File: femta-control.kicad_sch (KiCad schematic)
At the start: 19 parts, among them J1 CUBESAT INTERFACE

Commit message: work
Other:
- added sheet Valves (valve-master.kicad_sch)
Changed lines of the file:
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@@
+	)
+	(sheet
+		(at 292.1 91.44)
+		(size 40.64 29.21)
+		(fields_autoplaced yes)
+		(stroke
+			(width 0.1524)
+			(type solid)
+		)
+		(fill
+			(color 0 0 0 0.0000)
+		)
+		(property "Sheetname" "Valves"
+			(at 292.1 90.7284 0)
+			(effects
+				(font
+					(size 1.27 1.27)
+				)
+				(justify left bottom)
+			)
+		)
+		(property "Sheetfile" "valve-master.kicad_sch"
+			(at 292.1 121.2346 0)
+			(effects
+				(font
+					(size 1.27 1.27)
+				)
+				(justify left top)
+			)
+		)
+		(instances
+			(project "femta-control"
+				(path "/838bf11c-36b7-41d7-9462-fe98a188d617"
+					(page "31")
+				)
+			)
+		)
 	)
 	(sheet

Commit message: lots and lots and lots of work
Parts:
- added C94, C95: 10uF, symbol Device:C
- added U92: NCV1117-12_SOT223, Package_TO_SOT_SMD:SOT-223-3_TabPin2, symbol Regulator_Linear:NCP1117-12_SOT223
- R11: value 10K -> 24K
- R13: value 30K -> 24K
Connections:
- net +BATT: now also C94.1, U92.3 (VI)
- net GND: now also C94.2, C95.1, U92.1 (GND)
- new net +12V: C95.2, U92.2 (VO)
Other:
- sheet DPT Sensors renamed DPT and Flow
- sheet DPT and Flow: file dpt.kicad_sch -> dpt-flow.kicad_sch
- note added: "0.6A Limit on 3.3V Rail"
- note added: "0.6A Limit on 5V Rail"
- note added: "2.04A Limit on Batt Rail"
- note added: "2.04A Limit on Heater Rail"

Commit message: work
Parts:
- added JP2: HEATER_POWER, symbol Jumper:SolderJumper_2_Open
- added TP1: 5VTP, symbol Connector:TestPoint
- added TP2: 3V3TP, symbol Connector:TestPoint
- added TP3: 5VPTP, symbol Connector:TestPoint
- added TP4: BATTTP, symbol Connector:TestPoint
- added TP5: GNDTP, symbol Connector:TestPoint
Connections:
- net +3.3V: now also TP2.1
- net +5V: now also TP1.1
- net +5VP: now also TP3.1
- net +BATT: now also TP4.1
- net 5V_HEATER_UNPROT: now also JP2.2 (B)
- net 5V_UNPROT: now also JP2.1 (A)
- net GND: now also TP5.1
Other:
- note added: "Power indicators & Test Points"
- note removed: "Power indicators"

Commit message: 540 COMPONENTS I AM LOSING MY MINDDDDDD
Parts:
- added C3, C5, C6: 0.1uF, symbol Device:C
- added C4: 1uF, symbol Device:C
- added U2: MAX6103, Package_TO_SOT_SMD:SOT-23, symbol Reference_Voltage:MAX6103
- added U3: MCP3204, Package_SO:TSSOP-14_4.4x5mm_P0.65mm, symbol Analog_ADC:MCP3204
- TP1: footprint (none) -> TestPoint:TestPoint_Pad_D2.0mm
- TP2: renamed from TP5; footprint (none) -> TestPoint:TestPoint_Pad_D2.0mm
- TP3: renamed from TP2; footprint (none) -> TestPoint:TestPoint_Pad_D2.0mm
- TP4: renamed from TP3; footprint (none) -> TestPoint:TestPoint_Pad_D2.0mm
- TP5: renamed from TP4; footprint (none) -> TestPoint:TestPoint_Pad_D2.0mm
- renumbered C94 to C1, C95 to C2, JP2 to JP1, R6 to R1, R9 to R10, R7 to R2, R8 to R3, R10 to R4, R1 to R5, R2 to R6, R3 to R7, R4 to R8, R5 to R9, U92 to U1
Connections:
- net +3.3V: now also C6.1, U3.14 (Vdd)
- net +5V: now also C3.1, U2.1 (IN)
- net GND: now also C3.2, C4.2, C5.2, C6.2, U2.3 (GND), U3.12 (AGND), U3.3 (CH2), U3.4 (CH3), U3.7 (DGND)
- new net 3V_REF: C4.1, C5.1, U2.2 (OUT), U3.13 (Vref)
- new net I_TELEM_CS: U3.8 (~{CS}/SHDN)
- new net POUT_1: U3.1 (CH0)
- new net POUT_2: U3.2 (CH1)
- new net SPI_CLK: U3.11 (CLK)
- new net SPI_MISO: U3.10 (Dout)
- new net SPI_MOSI: U3.9 (Din)
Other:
- sheet Thermal Circuits ports: added 165_CS, 595_CS, EN_OUT_595, LOAD_165, LOAD_595, P_ADC_CS, SPI_CLK, SPI_MISO, SPI_MOSI, TSET_CS, T_ADC_CS; removed none
- sheet Thrust Control Side 1 ports: added POUT_CS, PSET_CS, SPI_CLK, SPI_MISO, SPI_MOSI; removed none
- sheet Thrust Control Side 2 ports: added POUT_CS, PSET_CS, SPI_CLK, SPI_MISO, SPI_MOSI; removed none
- sheet Thruster Control Main ports: added POUT_CS, PSET_CS, SPI_CLK, SPI_MISO, SPI_MOSI; removed none
- sheet Valves ports: added 595_CS, EN_OUT_595, LOAD_595, SPI_CLK, SPI_MOSI; removed none
- moved on the sheet: C1, C2, D1, D2, D3, D4, J1, JP1, R1, R10, R11, R12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

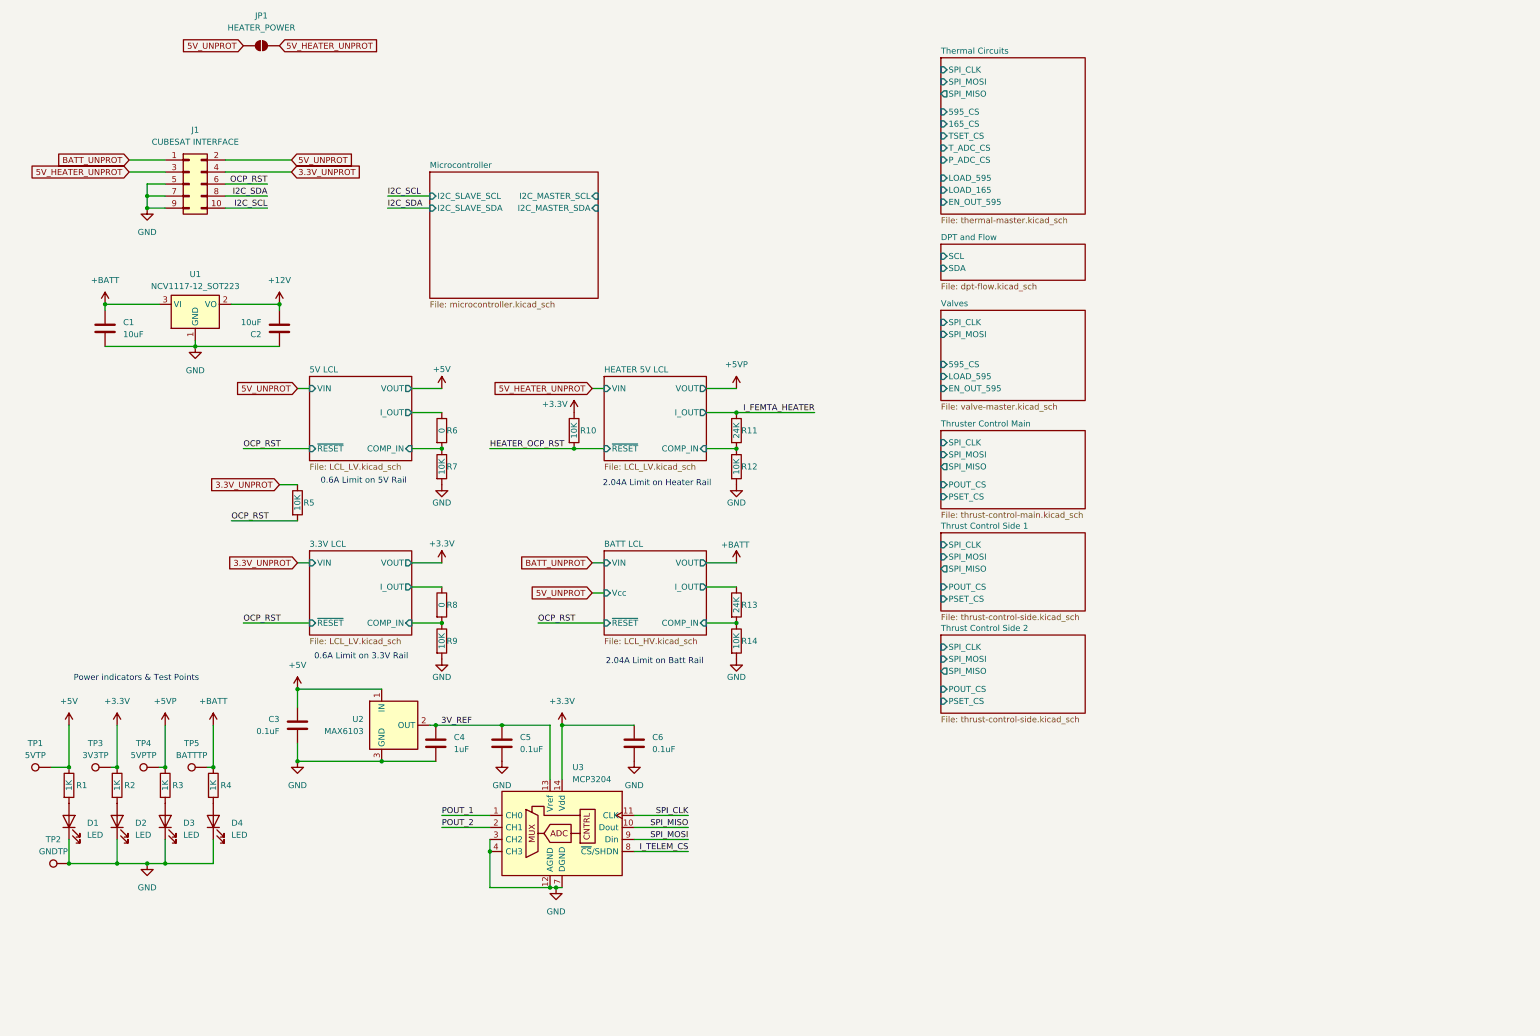
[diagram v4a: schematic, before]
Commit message: page sizes
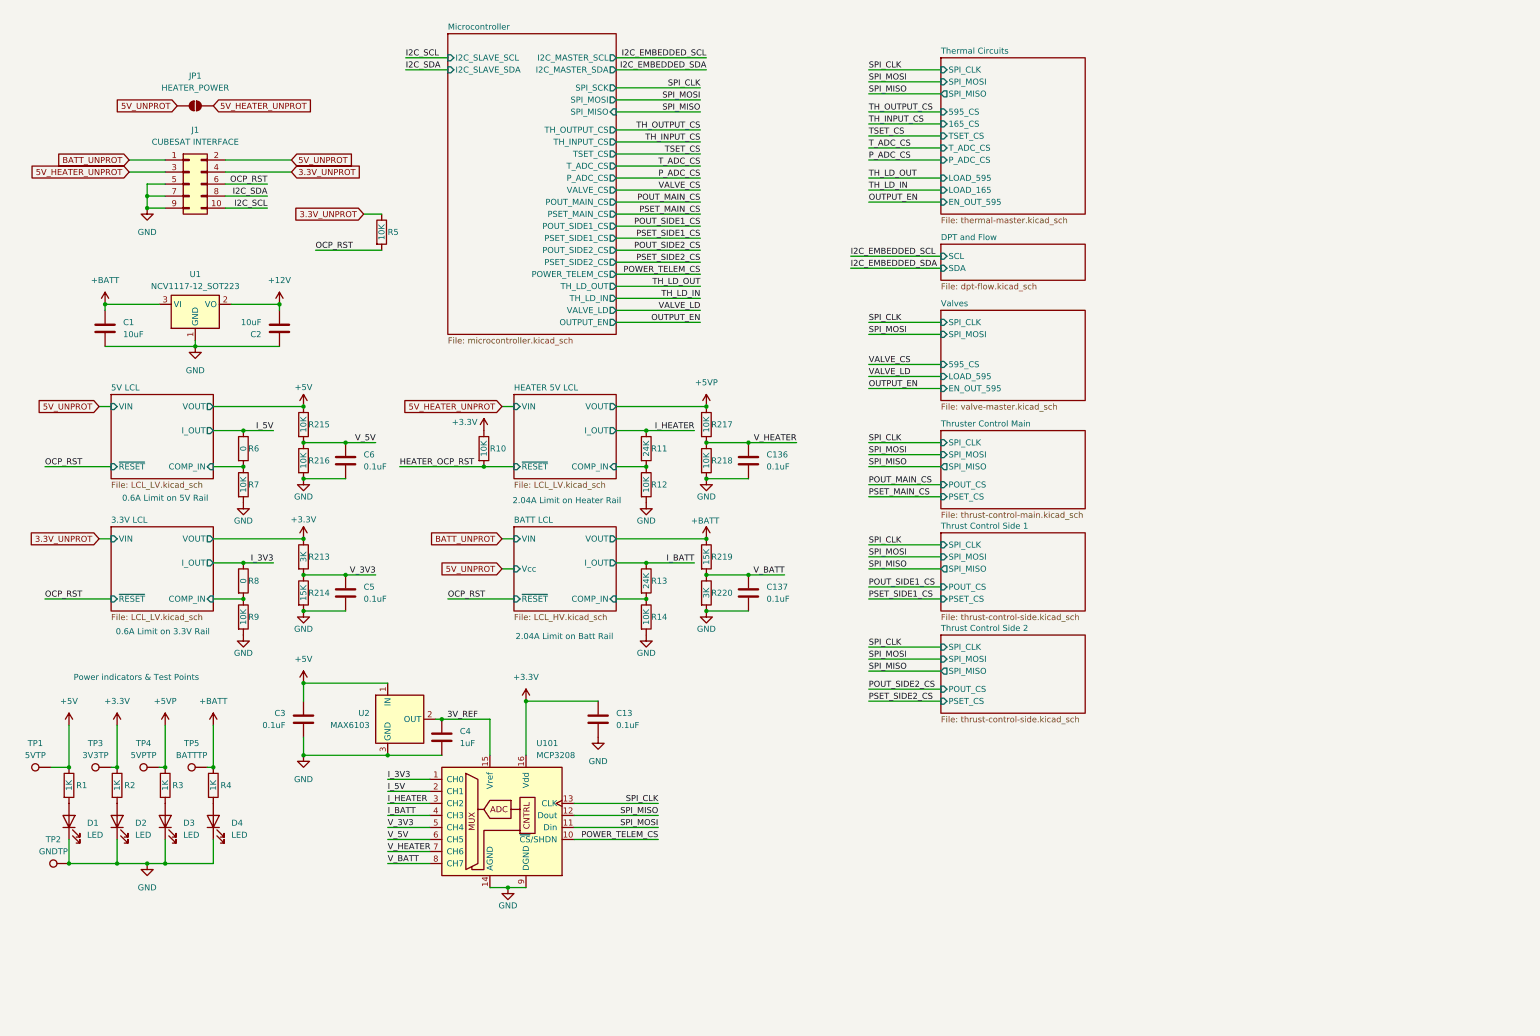
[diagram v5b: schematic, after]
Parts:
- removed U3: MCP3204, Package_SO:TSSOP-14_4.4x5mm_P0.65mm, symbol Analog_ADC:MCP3204
- added C13, C136, C137: 0.1uF, symbol Device:C
- added R213, R220: 3K, symbol Device:R
- added R214, R219: 15K, symbol Device:R
- added R215, R216, R217, R218: 10K, symbol Device:R
- added U101: MCP3208, Package_SO:SOIC-16_3.9x9.9mm_P1.27mm, symbol Analog_ADC:MCP3208
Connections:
- net +3.3V: now also C13.1, R213.1, U101.16 (Vdd); no longer C6.1
- net +5V: now also R215.1
- net +5VP: now also R217.1
- net +BATT: now also R219.1
- net 3V_REF: now also U101.15 (Vref); no longer C5.1
- net GND: now also C13.2, C136.2, C137.2, R214.2, R216.2, R218.2, R220.2, U101.14 (AGND), U101.9 (DGND)
- net SPI_CLK: now also U101.13 (CLK)
- net SPI_MISO: now also U101.12 (Dout)
- net SPI_MOSI: now also U101.11 (Din)
- net 3.3V LCL/I_OUT renamed I_3V3
- net I_3V3: now also U101.1 (CH0)
- net 5V LCL/I_OUT renamed I_5V
- net I_5V: now also U101.2 (CH1)
- net BATT LCL/I_OUT renamed I_BATT
- net I_BATT: now also U101.4 (CH3)
- net I_FEMTA_HEATER renamed I_HEATER
- net I_HEATER: now also U101.3 (CH2)
- new net POWER_TELEM_CS: U101.10 (~{CS}/SHDN)
- new net V_3V3: C5.1, R213.2, R214.1, U101.5 (CH4)
- new net V_5V: C6.1, R215.2, R216.1, U101.6 (CH5)
- new net V_BATT: C137.1, R219.2, R220.1, U101.8 (CH7)
- new net V_HEATER: C136.1, R217.2, R218.1, U101.7 (CH6)
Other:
- sheet Microcontroller ports: added OUTPUT_EN, POUT_MAIN_CS, POUT_SIDE1_CS, POUT_SIDE2_CS, POWER_TELEM_CS, PSET_MAIN_CS, PSET_SIDE1_CS, PSET_SIDE2_CS, P_ADC_CS, SPI_MISO, SPI_MOSI, SPI_SCK, TH_INPUT_CS, TH_LD_IN, TH_LD_OUT, TH_OUTPUT_CS, TSET_CS, T_ADC_CS, VALVE_CS, VALVE_LD; removed none
- moved on the sheet: C3, C4, JP1, R10, R11, R12, R13, R14, R5, R6, R7, R8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

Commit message: schematic finished milestone
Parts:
- renumbered C6 to C4, C4 to C6, C13 to C7, C136 to C8, C137 to C9, R216 to R10, R213 to R11, R214 to R12, R5 to R13, R10 to R14, R11 to R15, R12 to R16, R13 to R17, R14 to R18, R217 to R19, R218 to R20, R219 to R21, R220 to R22, R6 to R5, R7 to R6, R8 to R7, R9 to R8, R215 to R9, U101 to U3

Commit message: capacitor footprints
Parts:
- C1, C2: footprint (none) -> Capacitor_SMD:C_1210_3225Metric
- C3, C4, C5, C6, C7, C8, C9: footprint (none) -> Capacitor_SMD:C_0603_1608Metric
- D1, D2, D3, D4: footprint (none) -> Diode_SMD:D_0603_1608Metric
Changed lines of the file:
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@@
 			)
 		)
-		(property "Footprint" ""
+		(property "Footprint" "Capacitor_SMD:C_0603_1608Metric"
 			(at 141.9352 165.1 0)
 			(effects
@@
 			)
 		)
-		(property "Footprint" ""
+		(property "Footprint" "Capacitor_SMD:C_0603_1608Metric"
 			(at 88.5952 138.43 0)
 			(effects
@@
 			)
 		)
-		(property "Footprint" ""
+		(property "Footprint" "Capacitor_SMD:C_0603_1608Metric"
 			(at 173.6852 110.49 0)
 			(effects
@@
 			)
 		)
-		(property "Footprint" ""
+		(property "Footprint" "Capacitor_SMD:C_0603_1608Metric"
 			(at 173.6852 138.43 0)
 			(effects
@@
 			)
 		)
-		(property "Footprint" ""
+		(property "Footprint" "Diode_SMD:D_0603_1608Metric"
 			(at 49.53 182.88 0)
 			(effects
@@
 			)
 		)
-		(property "Footprint" ""
+		(property "Footprint" "Diode_SMD:D_0603_1608Metric"
 			(at 29.21 182.88 0)
 			(effects
@@
 			)
 		)
-		(property "Footprint" ""
+		(property "Footprint" "Diode_SMD:D_0603_1608Metric"
 			(at 39.37 182.88 0)
 			(effects
@@
 			)
 		)
-		(property "Footprint" ""
+		(property "Footprint" "Capacitor_SMD:C_0603_1608Metric"
 			(at 108.9152 168.91 0)
 			(effects
@@
 			)
 		)
-		(property "Footprint" ""
+		(property "Footprint" "Diode_SMD:D_0603_1608Metric"
 			(at 59.69 182.88 0)
 			(effects
@@
 			)
 		)
-		(property "Footprint" ""
+		(property "Footprint" "Capacitor_SMD:C_1210_3225Metric"
 			(at 37.7952 82.55 0)
 			(effects
@@
 			)
 		)
-		(property "Footprint" ""
+		(property "Footprint" "Capacitor_SMD:C_0603_1608Metric"
 			(at 79.7052 165.1 0)
 			(effects
@@
 			)
 		)
-		(property "Footprint" ""
+		(property "Footprint" "Capacitor_SMD:C_1210_3225Metric"
 			(at 72.6948 74.93 0)
 			(effects
@@
 			)
 		)
-		(property "Footprint" ""
+		(property "Footprint" "Capacitor_SMD:C_0603_1608Metric"
 			(at 88.5952 110.49 0)
 			(effects

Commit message: add more footprints
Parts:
- R1, R10, R11, R12, R13, R14, R15, R16, R17, R18, R19, R2, R20, R21, R22, R3, R4, R5, R6, R7, R8, R9: footprint (none) -> Resistor_SMD:R_0603_1608Metric
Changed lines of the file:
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@@
 			)
 		)
-		(property "Footprint" ""
+		(property "Footprint" "Resistor_SMD:R_0603_1608Metric"
 			(at 64.262 132.08 90)
 			(effects
@@
 			)
 		)
-		(property "Footprint" ""
+		(property "Footprint" "Resistor_SMD:R_0603_1608Metric"
 			(at 93.472 58.42 90)
 			(effects
@@
 			)
 		)
-		(property "Footprint" ""
+		(property "Footprint" "Resistor_SMD:R_0603_1608Metric"
 			(at 162.052 99.06 90)
 			(effects
@@
 			)
 		)
-		(property "Footprint" ""
+		(property "Footprint" "Resistor_SMD:R_0603_1608Metric"
 			(at 149.352 111.76 90)
 			(effects
@@
 			)
 		)
-		(property "Footprint" ""
+		(property "Footprint" "Resistor_SMD:R_0603_1608Metric"
 			(at 76.962 134.62 90)
 			(effects
@@
 			)
 		)
-		(property "Footprint" ""
+		(property "Footprint" "Resistor_SMD:R_0603_1608Metric"
 			(at 149.352 132.08 90)
 			(effects
@@
 			)
 		)
-		(property "Footprint" ""
+		(property "Footprint" "Resistor_SMD:R_0603_1608Metric"
 			(at 162.052 134.62 90)
 			(effects
@@
 			)
 		)
-		(property "Footprint" ""
+		(property "Footprint" "Resistor_SMD:R_0603_1608Metric"
 			(at 149.352 139.7 90)
 			(effects
@@
 			)
 		)
-		(property "Footprint" ""
+		(property "Footprint" "Resistor_SMD:R_0603_1608Metric"
 			(at 162.052 106.68 90)
 			(effects
@@
 			)
 		)
-		(property "Footprint" ""
+		(property "Footprint" "Resistor_SMD:R_0603_1608Metric"
 			(at 47.752 175.26 90)
 			(effects
@@
 			)
 		)
-		(property "Footprint" ""
+		(property "Footprint" "Resistor_SMD:R_0603_1608Metric"
 			(at 149.352 104.14 90)
 			(effects
@@
 			)
 		)
-		(property "Footprint" ""
+		(property "Footprint" "Resistor_SMD:R_0603_1608Metric"
 			(at 57.912 175.26 90)
 			(effects
@@
 			)
 		)
-		(property "Footprint" ""
+		(property "Footprint" "Resistor_SMD:R_0603_1608Metric"
 			(at 37.592 175.26 90)
 			(effects
@@
 			)
 		)
-		(property "Footprint" ""
+		(property "Footprint" "Resistor_SMD:R_0603_1608Metric"
 			(at 162.052 127 90)
 			(effects
@@
 			)
 		)
-		(property "Footprint" ""
+		(property "Footprint" "Resistor_SMD:R_0603_1608Metric"
 			(at 27.432 175.26 90)
 			(effects
@@
 			)
 		)
-		(property "Footprint" ""
+		(property "Footprint" "Resistor_SMD:R_0603_1608Metric"
 			(at 76.962 127 90)
 			(effects
@@
 			)
 		)
-		(property "Footprint" ""
+		(property "Footprint" "Resistor_SMD:R_0603_1608Metric"
 			(at 64.262 104.14 90)
 			(effects
@@
 			)
 		)
-		(property "Footprint" ""
+		(property "Footprint" "Resistor_SMD:R_0603_1608Metric"
 			(at 76.962 99.06 90)
 			(effects
@@
 			)
 		)
-		(property "Footprint" ""
+		(property "Footprint" "Resistor_SMD:R_0603_1608Metric"
 			(at 115.062 104.14 90)
 			(effects
@@
 			)
 		)
-		(property "Footprint" ""
+		(property "Footprint" "Resistor_SMD:R_0603_1608Metric"
 			(at 76.962 106.68 90)
 			(effects
@@
 			)
 		)
-		(property "Footprint" ""
+		(property "Footprint" "Resistor_SMD:R_0603_1608Metric"
 			(at 64.262 139.7 90)
 			(effects
@@
 			)
 		)
-		(property "Footprint" ""
+		(property "Footprint" "Resistor_SMD:R_0603_1608Metric"
 			(at 64.262 111.76 90)
 			(effects
